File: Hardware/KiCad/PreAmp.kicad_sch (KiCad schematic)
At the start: 1 part, among them U1 OPA1656ID

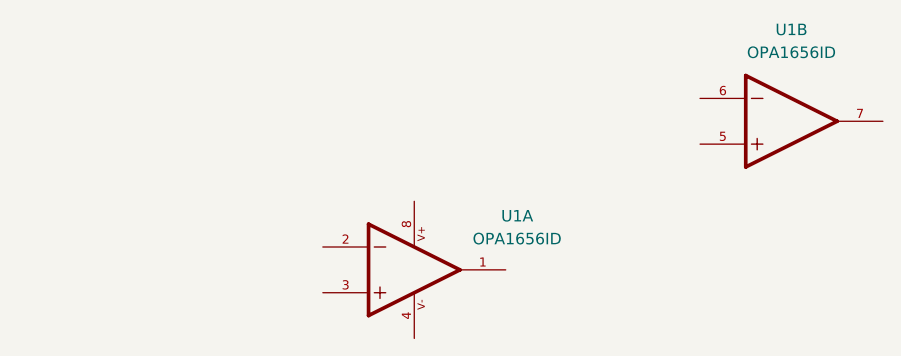
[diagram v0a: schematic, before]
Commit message: Re-orginanisation
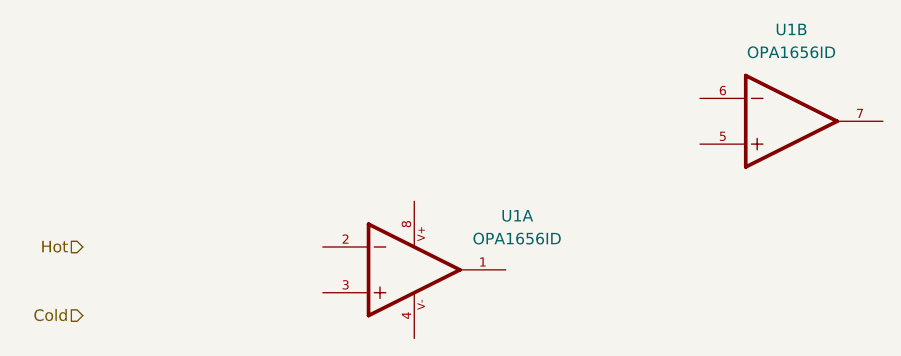
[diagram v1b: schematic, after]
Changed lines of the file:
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@@
 (kicad_sch
-	(version 20231120)
+	(version 20250114)
 	(generator "eeschema")
-	(generator_version "8.0")
+	(generator_version "9.0")
 	(paper "A4")
 	(title_block
@@
 		(company "Sounds Like Tim")
 	)
+	(hierarchical_label "Hot"
+		(shape input)
+		(at 66.04 91.44 180)
+		(effects
+			(font
+				(size 1.27 1.27)
+			)
+			(justify right)
+		)
+	)
+	(hierarchical_label "Cold"
+		(shape input)
+		(at 66.04 99.06 180)
+		(effects
+			(font
+				(size 1.27 1.27)
+			)
+			(justify right)
+		)
+	)
 	(symbol
